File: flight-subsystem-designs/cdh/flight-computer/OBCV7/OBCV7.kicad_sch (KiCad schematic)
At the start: 43 parts, among them U1 BEAGLEBONEBLACK, U3 TCAN337G, U4 MCP7940N-xSN, U5 ADM3485EARZ, U6 MAX706RESA+T, U7 TMP36xS

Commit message: New Board Version with better Signal Integrity
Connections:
- net CAN_FAULT: now also U1.P8_14 (GPIO0_26); no longer U1.P8_37 (UART5_TXD)
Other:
- moved on the sheet: BT1, C1, C10, C11, C12, C2, C3, C4, C5, C6, C7, C8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

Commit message: Hopefully Final-ish Board
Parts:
- added 3V3: TestPoint, TestPoint:TestPoint_THTPad_D3.0mm_Drill1.5mm, symbol Connector:TestPoint
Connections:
- net SYS_5V: no longer C7.1, C9.1, D2.2 (A), H6.25 (Pin_25), H6.26 (Pin_26), U1.P9_5 (VDD_5V), U1.P9_6 (VDD_5V)
- net VDD_3V3B: now also 3V3.1
- new net VDD_5V: C7.1, C9.1, D2.2 (A), H6.25 (Pin_25), H6.26 (Pin_26), U1.P9_5 (VDD_5V), U1.P9_6 (VDD_5V)
- no-connect marks 108 -> 109
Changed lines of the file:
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@@
 	)
 	(junction
-		(at 92.71 20.32)
-		(diameter 0)
-		(color 0 0 0 0)
-	)
-	(junction
 		(at 90.17 25.4)
 		(diameter 0)
@@
 	)
 	(junction
+		(at 213.36 118.11)
+		(diameter 0)
+		(color 0 0 0 0)
+	)
+	(junction
 		(at 25.4 66.04)
 		(diameter 0)
@@
 	)
 	(no_connect
+		(at 88.9 22.86)
+	)
+	(no_connect
 		(at 210.82 41.91)
 	)
@@
 	(wire
 		(pts
-			(xy 88.9 22.86) (xy 92.71 22.86)
-		)
-		(stroke
-			(width 0)
-			(type default)
-		)
-	)
-	(wire
-		(pts
 			(xy 316.23 203.2) (xy 316.23 210.82)
 		)
@@
 	(wire
 		(pts
-			(xy 88.9 20.32) (xy 92.71 20.32)
+			(xy 88.9 20.32) (xy 96.52 20.32)
 		)
 		(stroke
@@
 	(wire
 		(pts
+			(xy 213.36 118.11) (xy 218.44 118.11)
+		)
+		(stroke
+			(width 0)
+			(type default)
+		)
+	)
+	(wire
+		(pts
 			(xy 189.23 205.74) (xy 189.23 229.87)
 		)
@@
 	(wire
 		(pts
-			(xy 92.71 20.32) (xy 96.52 20.32)
-		)
-		(stroke
-			(width 0)
-			(type default)
-		)
-	)
-	(wire
-		(pts
 			(xy 334.01 163.83) (xy 361.95 163.83)
 		)
@@
 	(wire
 		(pts
-			(xy 92.71 22.86) (xy 92.71 20.32)
-		)
-		(stroke
-			(width 0)
-			(type default)
-		)
-	)
-	(wire
-		(pts
 			(xy 318.77 43.18) (xy 330.2 43.18)
 		)
@@
 	(wire
 		(pts
-			(xy 210.82 118.11) (xy 218.44 118.11)
+			(xy 210.82 118.11) (xy 213.36 118.11)
 		)
 		(stroke
@@
 	)
 	(symbol
+		(lib_id "power:PWR_FLAG")
+		(at 213.36 118.11 180)
+		(unit 1)
+		(exclude_from_sim no)
+		(in_bom yes)
+		(on_board yes)
+		(dnp no)
+		(fields_autoplaced yes)
+		(property "Reference" "#FLG05"
+			(at 213.36 120.015 0)
+			(effects
+				(font
+					(size 1.27 1.27)
+				)
+				(hide yes)
+			)
+		)
+		(property "Value" "PWR_FLAG"
+			(at 213.36 123.19 0)
+			(effects
+				(font
+					(size 1.27 1.27)
+				)
+			)
+		)
+		(property "Footprint" ""
+			(at 213.36 118.11 0)
+			(effects
+				(font
+					(size 1.27 1.27)
+				)
+				(hide yes)
+			)
+		)
+		(property "Datasheet" "~"
+			(at 213.36 118.11 0)
+			(effects
+				(font
+					(size 1.27 1.27)
+				)
+				(hide yes)
+			)
+		)
+		(property "Description" "Special symbol for telling ERC where power comes from"
+			(at 213.36 118.11 0)
+			(effects
+				(font
+					(size 1.27 1.27)
+				)
+				(hide yes)
+			)
+		)
+		(pin "1"
+		)
+		(instances
+			(project ""
+				(path "/f39278fd-57d9-4bf0-96b9-1349133ef8a7"
+					(reference "#FLG05")
+					(unit 1)
+				)
+			)
+		)
+	)
+	(symbol
 		(lib_id "power:GND")
 		(at 389.89 198.12 0)
@@
 		(on_board yes)
 		(dnp no)
-		(fields_autoplaced yes)
 		(property "Reference" "BT1"
 			(at 182.3085 114.3 90)
@@
 					(unit 1)
 				)
+			)
+		)
+	)
+	(symbol
+		(lib_id "Connector:TestPoint")
+		(at 90.17 17.78 0)
+		(unit 1)
+		(exclude_from_sim no)
+		(in_bom yes)
+		(on_board yes)
+		(dnp no)
+		(fields_autoplaced yes)
+		(property "Reference" "3V3"
+			(at 92.71 13.2079 0)
+			(effects
+				(font
+					(size 1.27 1.27)
+				)
+				(justify left)
+			)
+		)
+		(property "Value" "TestPoint"
+			(at 92.71 15.7479 0)
+			(effects
+				(font
+					(size 1.27 1.27)
+				)
+				(justify left)
+			)
+		)
+		(property "Footprint" "TestPoint:TestPoint_THTPad_D3.0mm_Drill1.5mm"
+			(at 95.25 17.78 0)
+			(effects
+				(font
+					(size 1.27 1.27)
+				)
+				(hide yes)
+			)
+		)
+		(property "Datasheet" "~"
+			(at 95.25 17.78 0)
+			(effects
+				(font
+					(size 1.27 1.27)
+				)
+				(hide yes)
+			)
+		)
+		(property "Description" "test point"
+			(at 90.17 17.78 0)
+			(effects
+				(font
+					(size 1.27 1.27)
+				)
+				(hide yes)
+			)
+		)
+		(pin "1"
+		)
+		(instances
+			(project ""
+				(path "/f39278fd-57d9-4bf0-96b9-1349133ef8a7"
+					(reference "3V3")
+					(unit 1)
+				)

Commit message: It should be good this time guys trust
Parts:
- BT1: footprint Battery:BatteryHolder_Keystone_3034_1x20mm -> Battery:BatteryHolder_Keystone_106_1x20mm
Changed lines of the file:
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@@
 			)
 		)
-		(property "Footprint" "Battery:BatteryHolder_Keystone_3034_1x20mm"
+		(property "Footprint" "Battery:BatteryHolder_Keystone_106_1x20mm"
 			(at 182.626 121.92 90)
 			(effects

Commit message: obc changes'
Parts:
- U3: footprint Package_TO_SOT_SMD:TSOT-23-8 -> Footprints:TCAN337GD
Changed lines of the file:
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@@
 			)
 		)
-		(property "Footprint" "Package_TO_SOT_SMD:TSOT-23-8"
+		(property "Footprint" "Footprints:TCAN337GD"
 			(at 306.07 58.42 0)
 			(effects

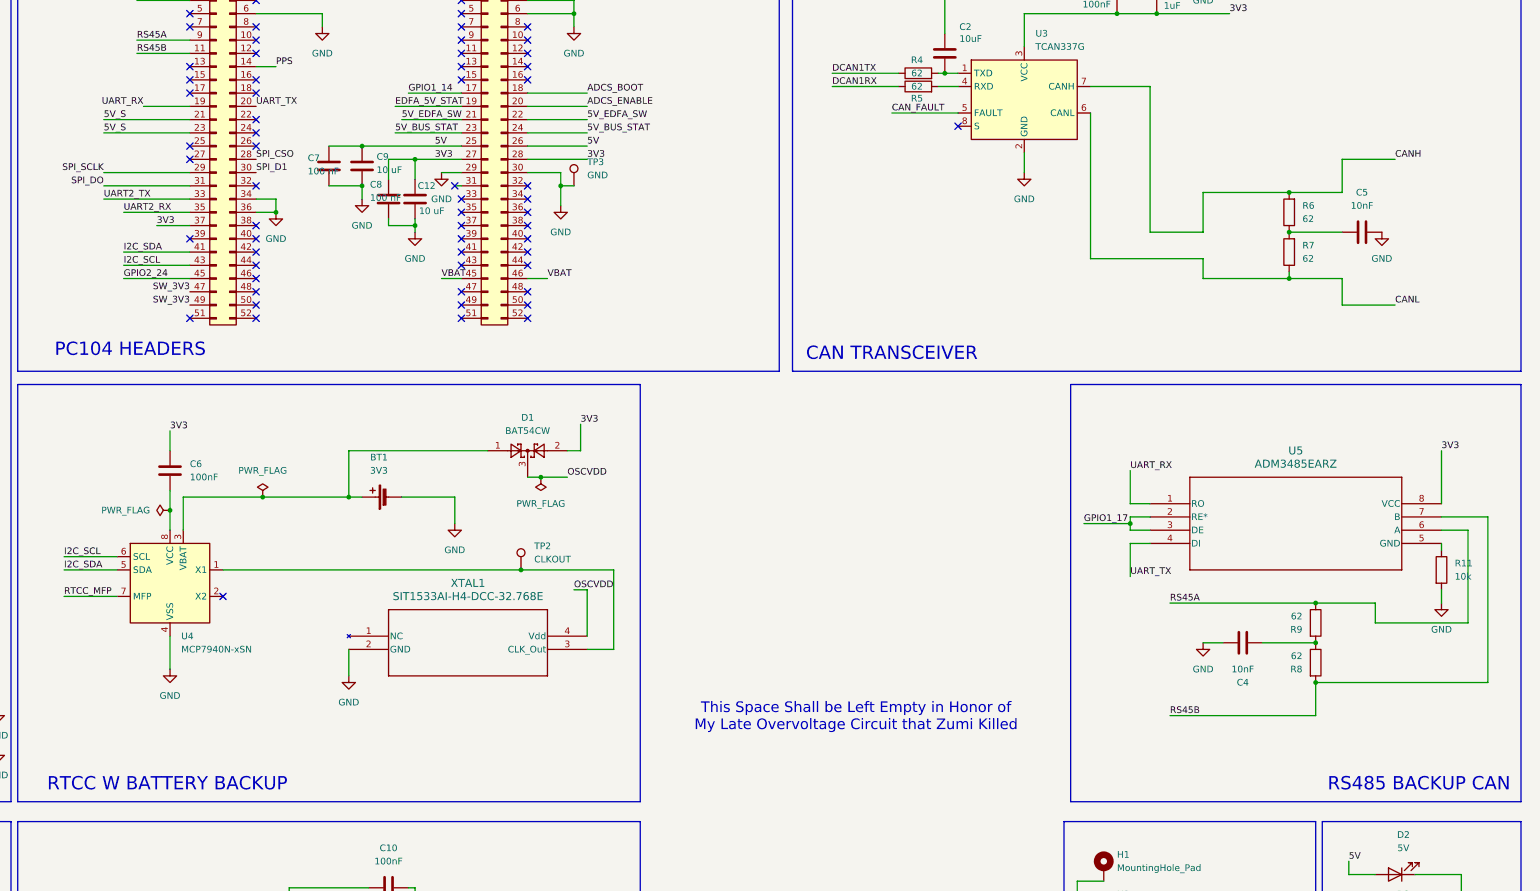
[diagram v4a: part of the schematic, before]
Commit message: Fixed UART
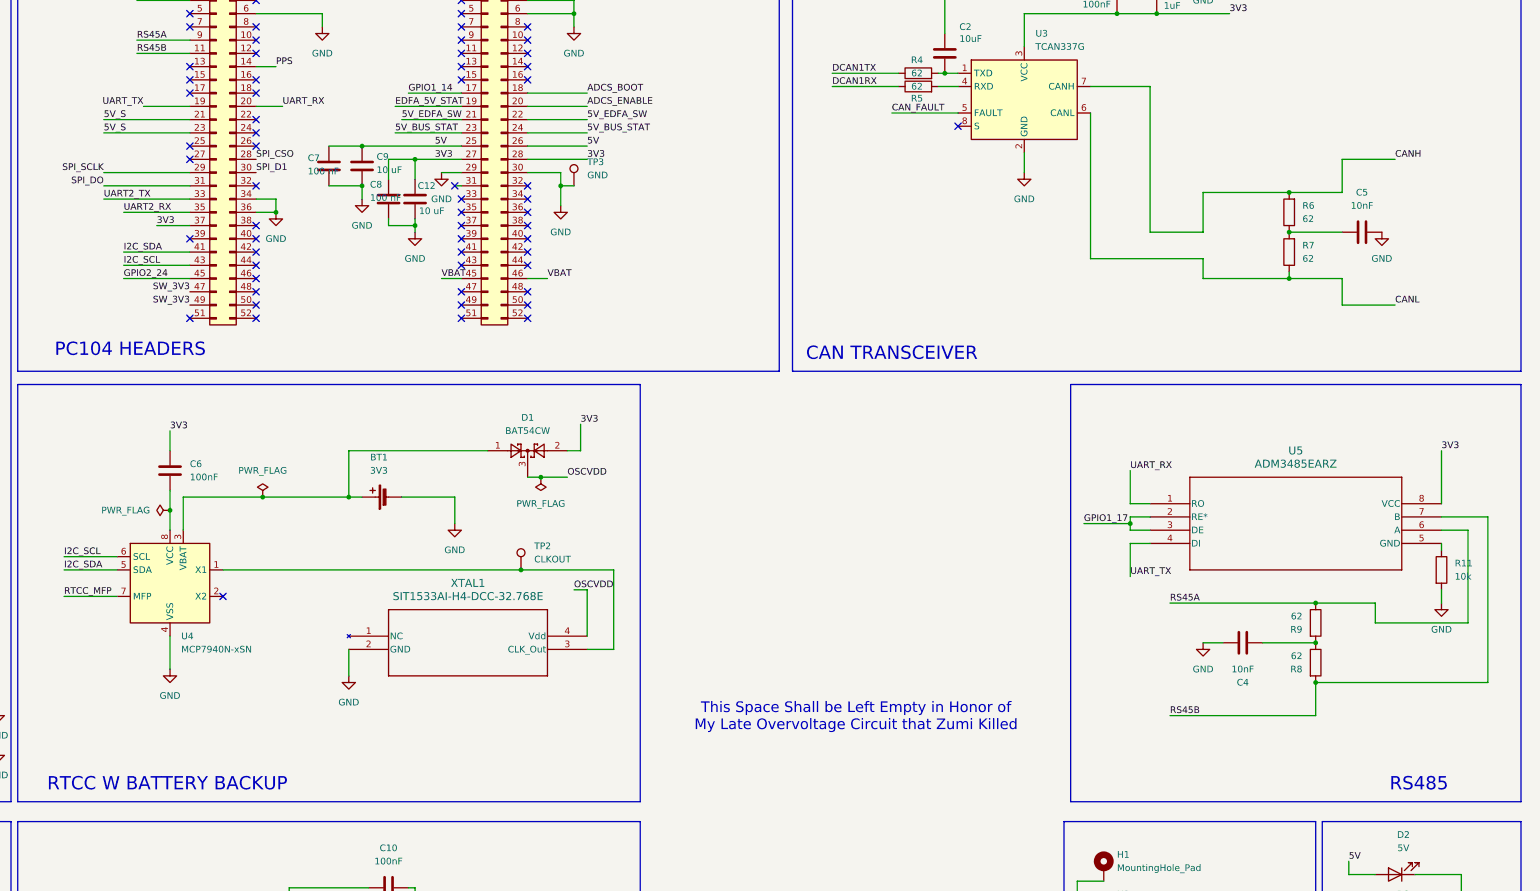
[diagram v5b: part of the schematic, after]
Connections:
- net UART_RX: now also H5.20 (Pin_20); no longer H5.19 (Pin_19)
- net UART_TX: now also H5.19 (Pin_19); no longer H5.20 (Pin_20)
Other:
- note added: "RS485"
- note removed: "RS485 BACKUP CAN"
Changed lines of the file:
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@@
 		)
 	)
-	(text "RS485 BACKUP CAN"
+	(text "RS485\n"
 		(exclude_from_sim no)
 		(at 381.762 177.038 0)
@@
 	(wire
 		(pts
+			(xy 163.83 46.99) (xy 158.75 46.99)
+		)
+		(stroke
+			(width 0)
+			(type default)
+		)
+	)
+	(wire
+		(pts
 			(xy 20.32 147.32) (xy 27.94 147.32)
 		)
@@
 		)
 	)
-	(label "UART_TX"
-		(at 158.75 46.99 0)
+	(label "UART_RX"
+		(at 163.83 46.99 0)
 		(effects
 			(font
@@
 		)
 	)
-	(label "UART_RX"
+	(label "UART_TX"
 		(at 137.16 46.99 180)
 		(effects
